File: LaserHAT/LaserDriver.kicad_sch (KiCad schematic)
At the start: 19 parts, among them J1 GPIO, U1 M24C32-WDW6TP, U4 MCP1700x-330xxMB

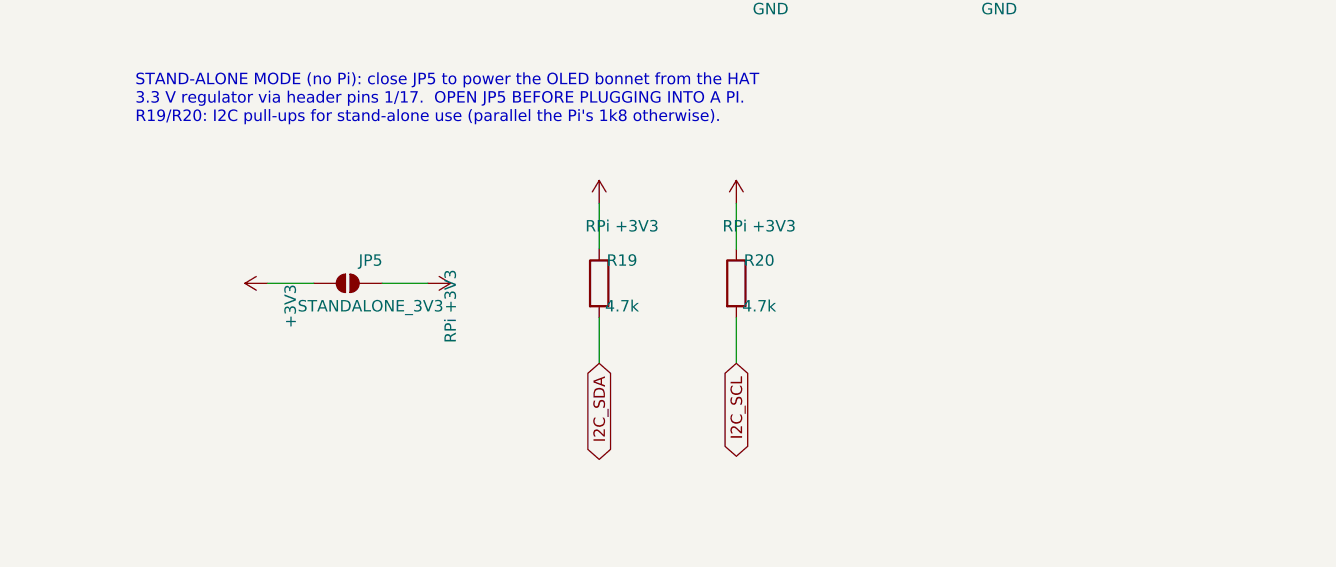
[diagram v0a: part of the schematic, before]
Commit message: BOM: descriptions from the LCSC catalog, value verifier and netlist-vs-board check on all three boards
R15 (2k, C4109) still said "200Ω" in its Description: the Rev 1 symbols carried descriptions and
datasheet links of parts long replaced (R13 "1kΩ", D5 "Emerald Green", D7 "Ice Blue", L1 "22uH 6x6",
Rs1 "10Ω", D3 "1N4148", ...). Now:
- tools/lcsc_catalog.json: LCSC MPN, brand, package, description, parameter table (Resistance /
  Capacitance / Inductance ...) and datasheet URL for every code, fetched by tools/lcsc_verify.py
- stamp_lcsc.py writes Description "<MPN> (<brand>, <package>): <LCSC description>" and the LCSC
  datasheet URL into every machine-placed symbol and footprint (HAT + laser)
- tools/lcsc_verify.py: every R/C/L Value must equal LCSC's parameter, other parts' MPN must match
  the Value (label values like "FIRE" are listed, not failed), size codes must match the package;
  covers HAT, laser and the e-stim list (bom_EStimDaughter.csv) and the fields the toolkit reads:
  0 mismatches on all three boards
- tools/sync_check.py: read-only F8 (parts, footprint ids, values, DNP, pad nets, paths vs the
  exported netlist): 0 differences on all three boards after fixing the owl's missing
  "Footprints:" library prefix and the e-stim U5/U8 paths (netlist uses the other unit's uuid;
  backup in stash/EStimDaughter_2026-09-30_pre-unitpath.kicad_pcb)
- values: laser D1/D3 "SS14" -> "DSK14" (the part ordered), HAT J5 -> "GT-USB-7010ASV"
- fab outputs regenerated; ERC/DRC unchanged

Co-Authored-By: Claude Fable 5.1 <noreply@anthropic.com>
Claude-Session: https://claude.ai/code/session_018vgLizGzYPynnY93ajvoVA
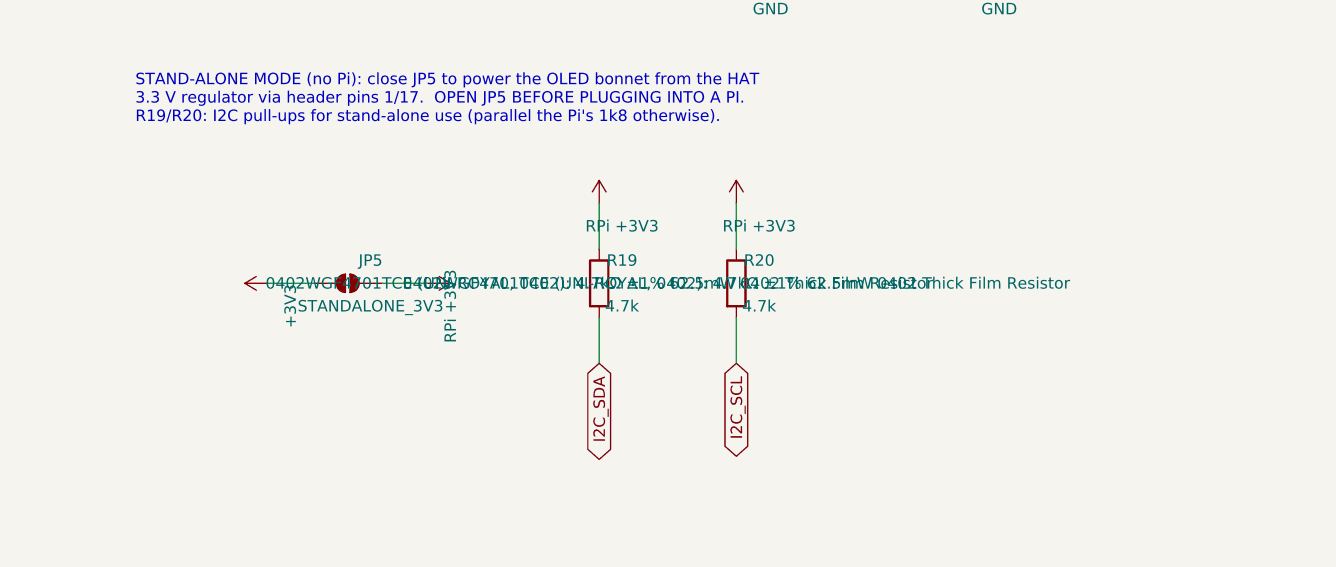
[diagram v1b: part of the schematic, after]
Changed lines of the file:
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@@
 			)
 		)
-		(property "Datasheet" "~"
+		(property "Datasheet" "https://datasheet.lcsc.com/datasheet/pdf/8238ae278d43fbd59fd57ef71ae67c27.pdf?productCode=C2290"
 			(at 275.59 127 0)
 			(effects
@@
 			)
 		)
-		(property "Description" "Emerald Green LED Indication - Discrete 3V 0603"
+		(property "Description" "KT-0603W (Hubei KENTO Elec, 0603): White LED Indication - Discrete 2.6V~3.1V 0603"
 			(at 275.59 127 0)
 			(effects
@@
 			)
 		)
-		(property "Datasheet" "~"
+		(property "Datasheet" "https://datasheet.lcsc.com/datasheet/pdf/02336ea48ea44ca18c72517dd3cb7b47.pdf?productCode=C307331"
 			(at 67.31 177.8 0)
 			(effects
@@
 			)
 		)
-		(property "Description" "100nF ±10% 50V Ceramic Capacitor X7R 0402"
+		(property "Description" "CL05B104KB54PNC (Samsung Electro-Mechanics, 0402): 100nF ±10% 50V Ceramic Capacitor X7R 0402"
 			(at 67.31 177.8 0)
 			(effects
@@
 			)
 		)
-		(property "Datasheet" "~"
+		(property "Datasheet" "https://datasheet.lcsc.com/datasheet/pdf/0a975aaa49b7c97f38a963127be4a823.pdf?productCode=C51721"
 			(at 93.98 170.18 0)
 			(effects
@@
 			)
 		)
-		(property "Description" "100mW 3.9kΩ Thick Film Resistor ±100ppm/℃ ±1% 0402 Chip Resistor - Surface Mount RoHS"
+		(property "Description" "0402WGF3901TCE (UNI-ROYAL, 0402): 3.9kΩ ±1% 62.5mW 0402 Thick Film Resistor"
 			(at 93.98 170.18 0)
 			(effects
@@
 			)
 		)
-		(property "Datasheet" "~"
+		(property "Datasheet" "https://datasheet.lcsc.com/datasheet/pdf/0a975aaa49b7c97f38a963127be4a823.pdf?productCode=C51721"
 			(at 101.6 170.18 0)
 			(effects
@@
 			)
 		)
-		(property "Description" "100mW 3.9kΩ Thick Film Resistor ±100ppm/℃ ±1% 0402 Chip Resistor - Surface Mount RoHS"
+		(property "Description" "0402WGF3901TCE (UNI-ROYAL, 0402): 3.9kΩ ±1% 62.5mW 0402 Thick Film Resistor"
 			(at 101.6 170.18 0)
 			(effects
@@
 			)
 		)
-		(property "Datasheet" ""
+		(property "Datasheet" "https://datasheet.lcsc.com/datasheet/pdf/0a975aaa49b7c97f38a963127be4a823.pdf?productCode=C25900"
 			(at 271.78 185.42 0)
 			(effects
@@
 			)
 		)
-		(property "Description" ""
+		(property "Description" "0402WGF4701TCE (UNI-ROYAL, 0402): 4.7kΩ ±1% 62.5mW 0402 Thick Film Resistor"
 			(at 271.78 185.42 0)
 			(effects
@@
 			)
 		)
-		(property "Datasheet" "https://www.onsemi.cn/PowerSolutions/document/CAT24C256-D.PDF"
+		(property "Datasheet" "https://datasheet.lcsc.com/datasheet/pdf/aa364b66c07e650f97701dabb6c06961.pdf?productCode=C283445"
 			(at 81.28 177.8 0)
 			(effects
@@
 			)
 		)
-		(property "Description" "32 kb CMOS Serial EEPROM, DIP-8/SOIC-8/TSSOP-8/DFN-8"
+		(property "Description" "M24C32-WDW6TP (ST, TSSOP-8): 32Kbit 1MHz I2C TSSOP-8 Memory"
 			(at 81.28 177.8 0)
 			(effects
@@
 			)
 		)
-		(property "Datasheet" "~"
+		(property "Datasheet" "https://datasheet.lcsc.com/datasheet/pdf/0a975aaa49b7c97f38a963127be4a823.pdf?productCode=C4109"
 			(at 300.99 140.97 0)
 			(effects
@@
 			)
 		)
-		(property "Description" "100mW 200Ω Thick Film Resistor ±100ppm/℃ ±1% 0402 Chip Resistor - Surface Mount RoHS"
+		(property "Description" "0402WGF2001TCE (UNI-ROYAL, 0402): 2kΩ ±1% 62.5mW 0402 Thick Film Resistor"
 			(at 300.99 140.97 0)
 			(effects
@@
 			)
 		)
-		(property "Datasheet" "http://ww1.microchip.com/downloads/en/DeviceDoc/20001826D.pdf"
+		(property "Datasheet" "https://datasheet.lcsc.com/datasheet/pdf/72cfd1a349d992af3a1c7bc40df24196.pdf?productCode=C632000"
 			(at 62.23 110.49 0)
 			(effects
@@
 			)
 		)
-		(property "Description" "250mA Low Quiscent Current LDO, 3.3V output, SOT-89"
+		(property "Description" "MCP1700T-3302E/MB (MICROCHIP, SOT-89-3): 3.3V Positive Fixed SOT-89-3 Voltage Regulators - Linear, Low Drop Out (LDO) Regulators RoHS"
 			(at 62.23 109.22 0)
 			(effects
@@
 			)
 		)
-		(property "Datasheet" ""
+		(property "Datasheet" "https://datasheet.lcsc.com/datasheet/pdf/0a975aaa49b7c97f38a963127be4a823.pdf?productCode=C25900"
 			(at 256.54 185.42 0)
 			(effects
@@
 			)
 		)
-		(property "Description" ""
+		(property "Description" "0402WGF4701TCE (UNI-ROYAL, 0402): 4.7kΩ ±1% 62.5mW 0402 Thick Film Resistor"
 			(at 256.54 185.42 0)
 			(effects
@@
 			)
 		)
-		(property "Datasheet" "~"
+		(property "Datasheet" "https://datasheet.lcsc.com/datasheet/pdf/02336ea48ea44ca18c72517dd3cb7b47.pdf?productCode=C52923"
 			(at 76.2 113.03 0)
 			(effects
@@
 			)
 		)
-		(property "Description" "1uF ±10% 10V Ceramic Capacitor X7R 0402"
+		(property "Description" "CL05A105KA5NQNC (Samsung Electro-Mechanics, 0402): 1uF ±10% 25V Ceramic Capacitor X5R 0402"
 			(at 76.2 113.03 0)
 			(effects
@@
 			)
 		)
-		(property "Datasheet" "~"
+		(property "Datasheet" "https://datasheet.lcsc.com/datasheet/pdf/0a975aaa49b7c97f38a963127be4a823.pdf?productCode=C4109"
 			(at 275.59 140.97 0)
 			(effects
@@
 			)
 		)
-		(property "Description" "100mW 1kΩ 75V Thick Film Resistor ±100ppm/℃ ±1% 0402 Chip Resistor - Surface Mount RoHS"
+		(property "Description" "0402WGF2001TCE (UNI-ROYAL, 0402): 2kΩ ±1% 62.5mW 0402 Thick Film Resistor"
 			(at 275.59 140.97 0)
 			(effects
@@
 			)
 		)
-		(property "Datasheet" "~"
+		(property "Datasheet" "https://datasheet.lcsc.com/datasheet/pdf/0a975aaa49b7c97f38a963127be4a823.pdf?productCode=C25744"
 			(at 148.59 59.69 0)
 			(effects
@@
 			)
 		)
-		(property "Description" "200mW 10kΩ Thick Film Resistor ±100ppm/℃ ±1% 0402 Chip Resistor - Surface Mount RoHS"
+		(property "Description" "0402WGF1002TCE (UNI-ROYAL, 0402): 10kΩ ±1% 62.5mW 0402 Thick Film Resistor"
 			(at 148.59 59.69 0)
 			(effects
@@
 			)
 		)
-		(property "Datasheet" "~"
+		(property "Datasheet" "https://datasheet.lcsc.com/datasheet/pdf/02336ea48ea44ca18c72517dd3cb7b47.pdf?productCode=C307331"
 			(at 48.26 113.03 0)
 			(effects
@@
 			)
 		)
-		(property "Description" "100nF ±10% 50V Ceramic Capacitor X7R 0402"
+		(property "Description" "CL05B104KB54PNC (Samsung Electro-Mechanics, 0402): 100nF ±10% 50V Ceramic Capacitor X7R 0402"
 			(at 48.26 113.03 0)
 			(effects
@@
 			)
 		)
-		(property "Datasheet" "~"
+		(property "Datasheet" "https://datasheet.lcsc.com/datasheet/pdf/011ec3e8cb1e825f6961d29bc4db4c7a.pdf?productCode=C2286"
 			(at 300.99 127 0)
 			(effects
@@
 			)
 		)
-		(property "Description" "Ice Blue LED Indication - Discrete 3.1V 0603"
+		(property "Description" "KT-0603R (Hubei KENTO Elec, 0603): Red 645nm LED Indication - Discrete 2.4V 0603"
 			(at 300.99 127 0)
 			(effects

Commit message: Fab: nothing JLC does not place may be in its BOM (hand-fitted and DNP parts excluded from BOM too)
JLC's upload rejects "R2,SW8,J1,J6,J7,J8,R1,J9 designators don't exist in the CPL file": a BOM
line without a placement is an error, not a "do not place". So HAND_FIT parts now carry symbol
"exclude from BOM" + footprint exclude-from-BOM and -position-files, NOT_FITTED parts DNP +
exclude-from-BOM (independent of the toolkit's "Exclude DNP" checkbox), e-stim PS1 likewise on
its board. jlc_fab.py classifies from lcsc_parts.HAND_FIT and warns on any flag drift.
Verified with the toolkit's own ProcessManager in both checkbox states: every BOM designator is
in the CPL on all three boards (HAT 30 lines / 42, laser 20 / 23, e-stim 23 / 42).

Co-Authored-By: Claude Fable 5.1 <noreply@anthropic.com>
Claude-Session: https://claude.ai/code/session_018vgLizGzYPynnY93ajvoVA
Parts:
- J1, R1, R2: now left out of the parts list
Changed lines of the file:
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@@
 		(unit 1)
 		(exclude_from_sim no)
-		(in_bom yes)
+		(in_bom no)
 		(on_board yes)
 		(dnp no)
@@
 		(unit 1)
 		(exclude_from_sim no)
-		(in_bom yes)
+		(in_bom no)
 		(on_board yes)
 		(dnp yes)
@@
 		(unit 1)
 		(exclude_from_sim no)
-		(in_bom yes)
+		(in_bom no)
 		(on_board yes)
 		(dnp yes)

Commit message: LaserHAT: SW8 BACK -> Panasonic EVQP7A01P side-actuated SMD (C79167); Values = part numbers; stamp clears flags
- SW8: schematic footprint Button_Switch_SMD:SW_SPST_EVQP7A; board footprint swapped at the south
  edge (111.55, 98.25), body flush with the edge, button ~0.35 mm proud; BUTTON1 via at the old
  THT pin joins the hand-routed B.Cu run, pad-1 pair bridged; GND pads on the pour. DRC identical
  to before the swap, 0 unconnected; backup stash/LaserDriver_user_2026-09-30_pre-sw8smd.kicad_pcb
- stamp_lcsc.py now also clears DNP / exclude flags on machine-placed parts (SW8 had stayed
  excluded after the previous commit, which wrongly claimed 43 placements)
- Values of LEDs and switches are the part numbers (KT-0603R/W, TS-1088-AR02016, MSK12C02,
  BL-DT, EVQP7A01P, PCM12SMTR) so JLC's BOM matcher sees one part per line; the function names
  remain as silkscreen texts
- verified: lcsc_verify 0 mismatches, sync_check 0 differences (HAT, laser), toolkit BOM/CPL
  consistent in both DNP modes (HAT 29 lines / 43 placements); fab outputs regenerated; docs

Co-Authored-By: Claude Fable 5.1 <noreply@anthropic.com>
Claude-Session: https://claude.ai/code/session_018vgLizGzYPynnY93ajvoVA
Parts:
- D5: value 5V -> KT-0603W
- D7: value MCU -> KT-0603R
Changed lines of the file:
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@@
 			)
 		)
-		(property "Value" "5V"
+		(property "Value" "KT-0603W"
 			(at 279.4 129.8574 90)
 			(effects
@@
 			)
 		)
-		(property "Value" "MCU"
+		(property "Value" "KT-0603R"
 			(at 304.8 129.8574 90)
 			(effects
